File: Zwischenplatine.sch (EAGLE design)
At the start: 8 parts

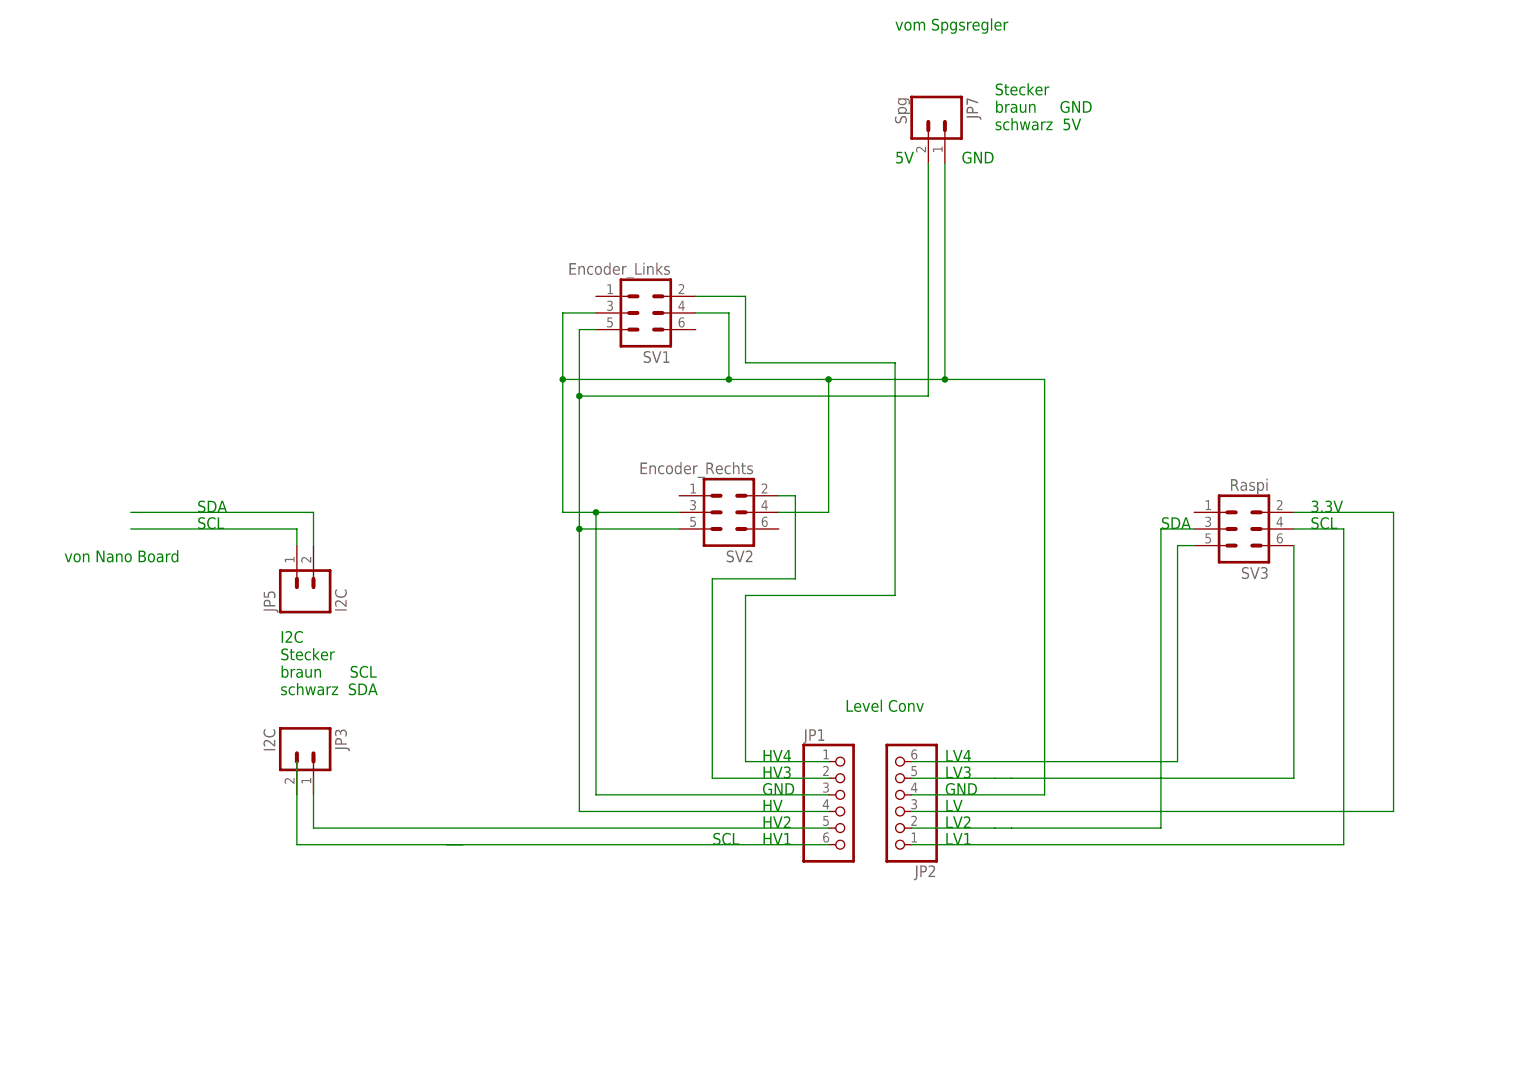
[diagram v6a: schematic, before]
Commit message: 
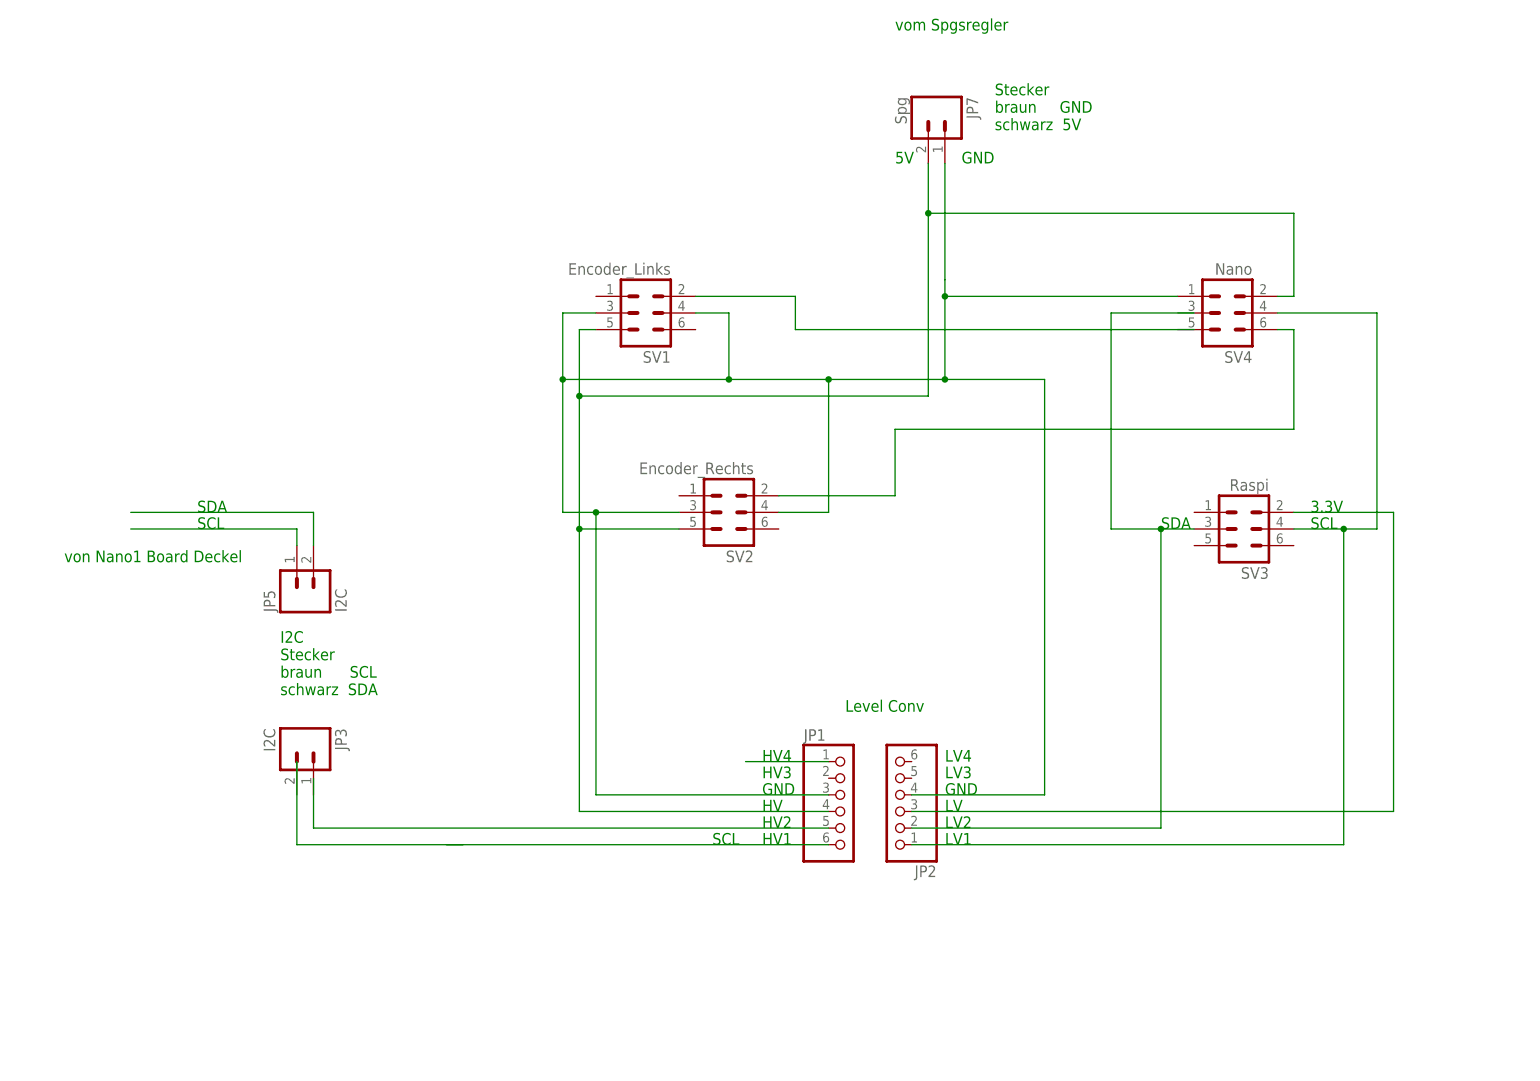
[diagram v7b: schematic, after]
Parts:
- added SV4: Nano, con-ml:ML6
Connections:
- removed net N$10: JP2.5, SV3.6
- removed net N$9: JP2.6, SV3.5
- new net N$3: JP1.1
- net N$1: now also SV4.2
- net N$11: now also SV4.1
- net N$14: now also SV4.4
- net PE4: no longer JP1.1
- net PE5: now also SV4.6; no longer JP1.2
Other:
- note added: "von Nano1 Board Deckel"
- note removed: "von Nano Board"
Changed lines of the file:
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@@
 <part name="JP3" library="SparkFun-Connectors" deviceset="M02" device="-JST-2MM-SMT" value="I2C"/>
 <part name="SV3" library="con-ml" deviceset="ML6" device="" value="Raspi"/>
+<part name="SV4" library="con-ml" deviceset="ML6" device="" value="Nano"/>
 </parts>
 <sheets>
@@
 braun      SCL
 schwarz  SDA</text>
-<text x="-73.66" y="78.74" size="1.778" layer="91">von Nano Board</text>
+<text x="-73.66" y="78.74" size="1.778" layer="91">von Nano1 Board Deckel</text>
 <text x="25.4" y="35.56" size="1.778" layer="91">SCL</text>
 <text x="116.84" y="83.82" size="1.778" layer="91">SCL</text>
@@
 <attribute name="NAME" x="110.49" y="77.978" size="1.778" layer="95" rot="R180"/>
 </instance>
+<instance part="SV4" gate="1" x="104.14" y="116.84" smashed="yes" rot="R180">
+<attribute name="VALUE" x="107.95" y="124.46" size="1.778" layer="96" rot="R180"/>
+<attribute name="NAME" x="107.95" y="110.998" size="1.778" layer="95" rot="R180"/>
+</instance>
 </instances>
 <busses>
@@
 <segment>
 <pinref part="SV2" gate="1" pin="2"/>
-<wire x1="35.56" y1="88.9" x2="38.1" y2="88.9" width="0.1524" layer="91"/>
-<pinref part="JP1" gate="A" pin="2"/>
-<wire x1="43.18" y1="45.72" x2="25.4" y2="45.72" width="0.1524" layer="91"/>
-<wire x1="25.4" y1="45.72" x2="25.4" y2="76.2" width="0.1524" layer="91"/>
-<wire x1="25.4" y1="76.2" x2="38.1" y2="76.2" width="0.1524" layer="91"/>
-<wire x1="38.1" y1="76.2" x2="38.1" y2="88.9" width="0.1524" layer="91"/>
+<wire x1="35.56" y1="88.9" x2="53.34" y2="88.9" width="0.1524" layer="91"/>
+<wire x1="53.34" y1="88.9" x2="53.34" y2="99.06" width="0.1524" layer="91"/>
+<wire x1="53.34" y1="99.06" x2="114.3" y2="99.06" width="0.1524" layer="91"/>
+<wire x1="114.3" y1="99.06" x2="114.3" y2="114.3" width="0.1524" layer="91"/>
+<pinref part="SV4" gate="1" pin="6"/>
+<wire x1="114.3" y1="114.3" x2="111.76" y2="114.3" width="0.1524" layer="91"/>
 </segment>
 </net>
 <net name="PE4" class="0">
 <segment>
-<wire x1="30.48" y1="119.38" x2="30.48" y2="109.22" width="0.1524" layer="91"/>
-<wire x1="30.48" y1="109.22" x2="53.34" y2="109.22" width="0.1524" layer="91"/>
-<wire x1="53.34" y1="109.22" x2="53.34" y2="73.66" width="0.1524" layer="91"/>
 <pinref part="SV1" gate="1" pin="2"/>
-<wire x1="30.48" y1="119.38" x2="22.86" y2="119.38" width="0.1524" layer="91"/>
-<pinref part="JP1" gate="A" pin="1"/>
-<wire x1="43.18" y1="48.26" x2="30.48" y2="48.26" width="0.1524" layer="91"/>
-<wire x1="30.48" y1="48.26" x2="30.48" y2="73.66" width="0.1524" layer="91"/>
-<wire x1="30.48" y1="73.66" x2="53.34" y2="73.66" width="0.1524" layer="91"/>
+<wire x1="22.86" y1="119.38" x2="38.1" y2="119.38" width="0.1524" layer="91"/>
+<wire x1="38.1" y1="119.38" x2="38.1" y2="114.3" width="0.1524" layer="91"/>
+<wire x1="38.1" y1="114.3" x2="99.06" y2="114.3" width="0.1524" layer="91"/>
 </segment>
 </net>
 <net name="N$1" class="3">
 <segment>
-<wire x1="58.42" y1="104.14" x2="58.42" y2="139.7" width="0.1524" layer="91"/>
+<wire x1="58.42" y1="104.14" x2="58.42" y2="132.08" width="0.1524" layer="91"/>
+<wire x1="58.42" y1="132.08" x2="58.42" y2="139.7" width="0.1524" layer="91"/>
 <wire x1="5.08" y1="114.3" x2="5.08" y2="104.14" width="0.1524" layer="91"/>
 <wire x1="5.08" y1="104.14" x2="5.08" y2="83.82" width="0.1524" layer="91"/>
@@
 <wire x1="5.08" y1="40.64" x2="43.18" y2="40.64" width="0.1524" layer="91"/>
 <junction x="5.08" y="83.82"/>
-</segment>
-</net>
-<net name="N$7" class="0">
-<segment>
-<pinref part="JP1" gate="A" pin="5"/>
-<wire x1="-35.56" y1="38.1" x2="-35.56" y2="45.72" width="0.1524" layer="91"/>
-<wire x1="43.18" y1="38.1" x2="-35.56" y2="38.1" width="0.1524" layer="91"/>
-</segment>
-</net>
-<net name="N$8" class="0">
-<segment>
-<pinref part="JP1" gate="A" pin="6"/>
-<wire x1="43.18" y1="35.56" x2="-15.24" y2="35.56" width="0.1524" layer="91"/>
-</segment>
-</net>
-<net name="N$9" class="0">
-<segment>
-<pinref part="JP2" gate="A" pin="6"/>
-<wire x1="55.88" y1="48.26" x2="96.52" y2="48.26" width="0.1524" layer="91"/>
-<wire x1="96.52" y1="48.26" x2="96.52" y2="81.28" width="0.1524" layer="91"/>
-<pinref part="SV3" gate="1" pin="5"/>
-<wire x1="96.52" y1="81.28" x2="99.06" y2="81.28" width="0.1524" layer="91"/>
-</segment>
-</net>
-<net name="N$10" class="0">
-<segment>
-<pinref part="JP2" gate="A" pin="5"/>
-<wire x1="55.88" y1="45.72" x2="68.58" y2="45.72" width="0.1524" layer="91"/>
-<pinref part="SV3" gate="1" pin="6"/>
-<wire x1="68.58" y1="45.72" x2="71.12" y2="45.72" width="0.1524" layer="91"/>
-<wire x1="71.12" y1="45.72" x2="114.3" y2="45.72" width="0.1524" layer="91"/>
-<wire x1="114.3" y1="45.72" x2="114.3" y2="81.28" width="0.1524" layer="91"/>
+<pinref part="SV4" gate="1" pin="2"/>
+<wire x1="111.76" y1="119.38" x2="114.3" y2="119.38" width="0.1524" layer="91"/>
+<wire x1="114.3" y1="119.38" x2="114.3" y2="132.08" width="0.1524" layer="91"/>
+<wire x1="114.3" y1="132.08" x2="58.42" y2="132.08" width="0.1524" layer="91"/>
+<junction x="58.42" y="132.08"/>
 </segment>
 </net>
@@
 <pinref part="JP1" gate="A" pin="3"/>
 <wire x1="43.18" y1="43.18" x2="7.62" y2="43.18" width="0.1524" layer="91"/>
-<wire x1="60.96" y1="139.7" x2="60.96" y2="106.68" width="0.1524" layer="91"/>
+<wire x1="60.96" y1="139.7" x2="60.96" y2="121.92" width="0.1524" layer="91"/>
 <pinref part="SV1" gate="1" pin="3"/>
+<wire x1="60.96" y1="119.38" x2="60.96" y2="106.68" width="0.1524" layer="91"/>
 <wire x1="7.62" y1="116.84" x2="2.54" y2="116.84" width="0.1524" layer="91"/>
 <wire x1="2.54" y1="116.84" x2="2.54" y2="106.68" width="0.1524" layer="91"/>
@@
 <wire x1="76.2" y1="106.68" x2="60.96" y2="106.68" width="0.1524" layer="91"/>
 <junction x="60.96" y="106.68"/>
+<pinref part="SV4" gate="1" pin="1"/>
+<wire x1="96.52" y1="119.38" x2="60.96" y2="119.38" width="0.1524" layer="91"/>
+<wire x1="60.96" y1="119.38" x2="60.96" y2="121.92" width="0.1524" layer="91"/>
+<junction x="60.96" y="119.38"/>
 </segment>
 </net>
@@
 <segment>
 <pinref part="JP2" gate="A" pin="2"/>
-<wire x1="55.88" y1="38.1" x2="68.58" y2="38.1" width="0.1524" layer="91"/>
 <pinref part="SV3" gate="1" pin="3"/>
-<wire x1="68.58" y1="38.1" x2="71.12" y2="38.1" width="0.1524" layer="91"/>
 <wire x1="99.06" y1="83.82" x2="93.98" y2="83.82" width="0.1524" layer="91"/>
 <wire x1="93.98" y1="83.82" x2="93.98" y2="38.1" width="0.1524" layer="91"/>
-<wire x1="93.98" y1="38.1" x2="71.12" y2="38.1" width="0.1524" layer="91"/>
+<wire x1="93.98" y1="38.1" x2="55.88" y2="38.1" width="0.1524" layer="91"/>
+<wire x1="93.98" y1="83.82" x2="86.36" y2="83.82" width="0.1524" layer="91"/>
+<wire x1="86.36" y1="83.82" x2="86.36" y2="116.84" width="0.1524" layer="91"/>
+<wire x1="86.36" y1="116.84" x2="99.06" y2="116.84" width="0.1524" layer="91"/>
+<junction x="93.98" y="83.82"/>
 </segment>
 </net>
@@
 <pinref part="SV3" gate="1" pin="4"/>
 <wire x1="121.92" y1="83.82" x2="114.3" y2="83.82" width="0.1524" layer="91"/>
+<pinref part="SV4" gate="1" pin="4"/>
+<wire x1="111.76" y1="116.84" x2="127" y2="116.84" width="0.1524" layer="91"/>
+<wire x1="127" y1="116.84" x2="127" y2="83.82" width="0.1524" layer="91"/>
+<wire x1="127" y1="83.82" x2="121.92" y2="83.82" width="0.1524" layer="91"/>
+<junction x="121.92" y="83.82"/>
 </segment>
 </net>
@@
 <net name="N$15" class="0">
 <segment>
-<wire x1="-12.7" y1="35.56" x2="-38.1" y2="35.56" width="0.1524" layer="91"/>
 <wire x1="-38.1" y1="35.56" x2="-38.1" y2="48.26" width="0.1524" layer="91"/>
-</segment>
-</net>
+<pinref part="JP1" gate="A" pin="6"/>
+<wire x1="43.18" y1="35.56" x2="-38.1" y2="35.56" width="0.1524" layer="91"/>
+</segment>
+</net>
+<net name="N$3" class="0">
+<segment>
+<pinref part="JP1" gate="A" pin="1"/>
+<wire x1="43.18" y1="48.26" x2="30.48" y2="48.26" width="0.1524" layer="91"/>
+</segment>
+</net>
+<net name="N$4" class="0">
+<segment>
+<pinref part="JP1" gate="A" pin="5"/>
+<wire x1="-35.56" y1="38.1" x2="-35.56" y2="45.72" width="0.1524" layer="91"/>
+<wire x1="43.18" y1="38.1" x2="-35.56" y2="38.1" width="0.1524" layer="91"/>
+</segment>
+</net>
+<net name="N$6" class="0">
+<segment>
+<wire x1="-12.7" y1="35.56" x2="-15.24" y2="35.56" width="0.1524" layer="91"/>
+</segment>
+</net>

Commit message: 
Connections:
- new net N$7: SV4.1
- new net N$9: SV2.1
- net N$1: no longer SV4.2
- net N$11: no longer SV4.1
- net PE4: now also SV4.2
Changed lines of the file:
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@@
 <pinref part="SV1" gate="1" pin="2"/>
 <wire x1="22.86" y1="119.38" x2="38.1" y2="119.38" width="0.1524" layer="91"/>
-<wire x1="38.1" y1="119.38" x2="38.1" y2="114.3" width="0.1524" layer="91"/>
-<wire x1="38.1" y1="114.3" x2="99.06" y2="114.3" width="0.1524" layer="91"/>
+<pinref part="SV4" gate="1" pin="2"/>
+<wire x1="111.76" y1="119.38" x2="114.3" y2="119.38" width="0.1524" layer="91"/>
+<wire x1="114.3" y1="119.38" x2="114.3" y2="132.08" width="0.1524" layer="91"/>
+<wire x1="114.3" y1="132.08" x2="38.1" y2="132.08" width="0.1524" layer="91"/>
+<wire x1="38.1" y1="132.08" x2="38.1" y2="119.38" width="0.1524" layer="91"/>
 </segment>
 </net>
 <net name="N$1" class="3">
 <segment>
-<wire x1="58.42" y1="104.14" x2="58.42" y2="132.08" width="0.1524" layer="91"/>
-<wire x1="58.42" y1="132.08" x2="58.42" y2="139.7" width="0.1524" layer="91"/>
+<wire x1="58.42" y1="104.14" x2="58.42" y2="139.7" width="0.1524" layer="91"/>
 <wire x1="5.08" y1="114.3" x2="5.08" y2="104.14" width="0.1524" layer="91"/>
 <wire x1="5.08" y1="104.14" x2="5.08" y2="83.82" width="0.1524" layer="91"/>
@@
 <wire x1="5.08" y1="40.64" x2="43.18" y2="40.64" width="0.1524" layer="91"/>
 <junction x="5.08" y="83.82"/>
-<pinref part="SV4" gate="1" pin="2"/>
-<wire x1="111.76" y1="119.38" x2="114.3" y2="119.38" width="0.1524" layer="91"/>
-<wire x1="114.3" y1="119.38" x2="114.3" y2="132.08" width="0.1524" layer="91"/>
-<wire x1="114.3" y1="132.08" x2="58.42" y2="132.08" width="0.1524" layer="91"/>
-<junction x="58.42" y="132.08"/>
 </segment>
 </net>
@@
 <pinref part="JP1" gate="A" pin="3"/>
 <wire x1="43.18" y1="43.18" x2="7.62" y2="43.18" width="0.1524" layer="91"/>
-<wire x1="60.96" y1="139.7" x2="60.96" y2="121.92" width="0.1524" layer="91"/>
+<wire x1="60.96" y1="139.7" x2="60.96" y2="106.68" width="0.1524" layer="91"/>
 <pinref part="SV1" gate="1" pin="3"/>
-<wire x1="60.96" y1="119.38" x2="60.96" y2="106.68" width="0.1524" layer="91"/>
 <wire x1="7.62" y1="116.84" x2="2.54" y2="116.84" width="0.1524" layer="91"/>
 <wire x1="2.54" y1="116.84" x2="2.54" y2="106.68" width="0.1524" layer="91"/>
@@
 <wire x1="76.2" y1="106.68" x2="60.96" y2="106.68" width="0.1524" layer="91"/>
 <junction x="60.96" y="106.68"/>
-<pinref part="SV4" gate="1" pin="1"/>
-<wire x1="96.52" y1="119.38" x2="60.96" y2="119.38" width="0.1524" layer="91"/>
-<wire x1="60.96" y1="119.38" x2="60.96" y2="121.92" width="0.1524" layer="91"/>
-<junction x="60.96" y="119.38"/>
 </segment>
 </net>
@@
 </segment>
 </net>
+<net name="N$7" class="0">
+<segment>
+<pinref part="SV4" gate="1" pin="1"/>
+<wire x1="96.52" y1="119.38" x2="45.72" y2="119.38" width="0.1524" layer="91"/>
+<wire x1="45.72" y1="119.38" x2="45.72" y2="129.54" width="0.1524" layer="91"/>
+<wire x1="45.72" y1="129.54" x2="2.54" y2="129.54" width="0.1524" layer="91"/>
+<wire x1="2.54" y1="129.54" x2="2.54" y2="119.38" width="0.1524" layer="91"/>
+<wire x1="2.54" y1="119.38" x2="10.16" y2="119.38" width="0.1524" layer="91"/>
+</segment>
+</net>
+<net name="N$9" class="0">
+<segment>
+<pinref part="SV2" gate="1" pin="1"/>
+<wire x1="20.32" y1="88.9" x2="12.7" y2="88.9" width="0.1524" layer="91"/>
+<wire x1="12.7" y1="88.9" x2="12.7" y2="101.6" width="0.1524" layer="91"/>
+<wire x1="12.7" y1="101.6" x2="93.98" y2="101.6" width="0.1524" layer="91"/>
+<wire x1="93.98" y1="101.6" x2="93.98" y2="114.3" width="0.1524" layer="91"/>
+<wire x1="93.98" y1="114.3" x2="99.06" y2="114.3" width="0.1524" layer="91"/>
+</segment>
+</net>
